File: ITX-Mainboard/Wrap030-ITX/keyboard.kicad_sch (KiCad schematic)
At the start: 4 parts, among them J13 DIN-6, U24 ATtiny2313A-PU, Y1 16M

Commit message: PCB substantial completion
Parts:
- removed J13: DIN-6, Wrap030-ITX:MiniDIN6, symbol Connector:DIN-6
- added J13: mDIN-6, Wrap030-ITX:MiniDIN6, symbol Wrap030-ITX:miniDIN-6 w/Shield
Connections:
- net GND: now also J13.0, J13.3
- net PS2-CLK: now also J13.5
- net PS2-DAT: now also J13.1
- net VCC: now also J13.4
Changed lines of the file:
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@@
     (stroke (width 0) (type default))
   )
-  (wire (pts (xy 109.22 162.56) (xy 119.38 162.56))
+  (wire (pts (xy 129.54 172.72) (xy 129.54 162.56))
     (stroke (width 0) (type default))
   )
@@
     (stroke (width 0) (type default))
   )
-  (wire (pts (xy 134.62 162.56) (xy 144.78 162.56))
+  (wire (pts (xy 137.16 149.86) (xy 147.32 149.86))
     (stroke (width 0) (type default))
   )
@@
     (effects (font (size 1.27 1.27)) (justify right bottom))
   )
-  (label "PS2-DAT" (at 109.22 162.56 0) (fields_autoplaced)
+  (label "PS2-DAT" (at 129.54 172.72 90) (fields_autoplaced)
     (effects (font (size 1.27 1.27)) (justify left bottom))
   )
@@
     (effects (font (size 1.27 1.27)) (justify left bottom))
   )
-  (label "PS2-CLK" (at 144.78 162.56 180) (fields_autoplaced)
+  (label "PS2-CLK" (at 147.32 149.86 180) (fields_autoplaced)
     (effects (font (size 1.27 1.27)) (justify right bottom))
   )
@@
     )
   )
-  (symbol (lib_id "power:VCC") (at 134.62 157.48 270) (unit 1)
-    (in_bom yes) (on_board yes) (dnp no) (fields_autoplaced)
-    (property "Reference" "#PWR03" (at 130.81 157.48 0)
-      (effects (font (size 1.27 1.27)) hide)
-    )
-    (property "Value" "VCC" (at 137.795 157.7968 90)
-      (effects (font (size 1.27 1.27)) (justify left))
-    )
-    (property "Footprint" "" (at 134.62 157.48 0)
-      (effects (font (size 1.27 1.27)) hide)
-    )
-    (property "Datasheet" "" (at 134.62 157.48 0)
+  (symbol (lib_id "power:VCC") (at 116.84 154.94 90) (unit 1)
+    (in_bom yes) (on_board yes) (dnp no) (fields_autoplaced)
+    (property "Reference" "#PWR03" (at 120.65 154.94 0)
+      (effects (font (size 1.27 1.27)) hide)
+    )
+    (property "Value" "VCC" (at 113.665 155.2568 90)
+      (effects (font (size 1.27 1.27)) (justify left))
+    )
+    (property "Footprint" "" (at 116.84 154.94 0)
+      (effects (font (size 1.27 1.27)) hide)
+    )
+    (property "Datasheet" "" (at 116.84 154.94 0)
       (effects (font (size 1.27 1.27)) hide)
     )
@@
     )
   )
-  (symbol (lib_id "power:GND") (at 127 152.4 180) (unit 1)
-    (in_bom yes) (on_board yes) (dnp no) (fields_autoplaced)
-    (property "Reference" "#PWR04" (at 127 146.05 0)
-      (effects (font (size 1.27 1.27)) hide)
-    )
-    (property "Value" "GND" (at 127 148.8981 0)
-      (effects (font (size 1.27 1.27)))
-    )
-    (property "Footprint" "" (at 127 152.4 0)
-      (effects (font (size 1.27 1.27)) hide)
-    )
-    (property "Datasheet" "" (at 127 152.4 0)
+  (symbol (lib_id "power:GND") (at 137.16 154.94 90) (unit 1)
+    (in_bom yes) (on_board yes) (dnp no) (fields_autoplaced)
+    (property "Reference" "#PWR04" (at 143.51 154.94 0)
+      (effects (font (size 1.27 1.27)) hide)
+    )
+    (property "Value" "GND" (at 140.335 155.2568 90)
+      (effects (font (size 1.27 1.27)) (justify right))
+    )
+    (property "Footprint" "" (at 137.16 154.94 0)
+      (effects (font (size 1.27 1.27)) hide)
+    )
+    (property "Datasheet" "" (at 137.16 154.94 0)
       (effects (font (size 1.27 1.27)) hide)
     )
@@
     )
   )
+  (symbol (lib_id "power:GND") (at 127 142.24 180) (unit 1)
+    (in_bom yes) (on_board yes) (dnp no) (fields_autoplaced)
+    (property "Reference" "#PWR04" (at 127 135.89 0)
+      (effects (font (size 1.27 1.27)) hide)
+    )
+    (property "Value" "GND" (at 127 138.7381 0)
+      (effects (font (size 1.27 1.27)))
+    )
+    (property "Footprint" "" (at 127 142.24 0)
+      (effects (font (size 1.27 1.27)) hide)
+    )
+    (property "Datasheet" "" (at 127 142.24 0)
+      (effects (font (size 1.27 1.27)) hide)
+    )
+    (pin "1")
+    (instances
+      (project "Wrap030-ITX"
+        (path "/911cb688-7d4c-4194-bbd3-2b645bd8d53c"
+          (reference "#PWR04") (unit 1)
+        )
+        (path "/911cb688-7d4c-4194-bbd3-2b645bd8d53c/26daa56c-062f-43fe-98ce-9d136969f1f9"
+          (reference "#PWR064") (unit 1)
+        )
+        (path "/911cb688-7d4c-4194-bbd3-2b645bd8d53c/b3cc5e75-f49f-4aac-aafa-9673c6f4863c"
+          (reference "#PWR0134") (unit 1)
+        )
+        (path "/911cb688-7d4c-4194-bbd3-2b645bd8d53c/aa0ccbb1-2ab7-4898-88a6-d9cd881bb239"
+          (reference "#PWR0174") (unit 1)
+        )
+        (path "/911cb688-7d4c-4194-bbd3-2b645bd8d53c/08245a1d-e019-4487-bc27-8c0c37f6c7e2"
+          (reference "#PWR0351") (unit 1)
+        )
+      )
+    )
+  )
   (symbol (lib_id "Device:Resonator_Small") (at 96.52 88.9 270) (unit 1)
     (in_bom yes) (on_board yes) (dnp no)
@@
     )
   )
-  (symbol (lib_id "power:VCC") (at 127 73.66 0) (unit 1)
-    (in_bom yes) (on_board yes) (dnp no) (fields_autoplaced)
-    (property "Reference" "#PWR03" (at 127 77.47 0)
-      (effects (font (size 1.27 1.27)) hide)
-    )
-    (property "Value" "VCC" (at 127 70.1581 0)
-      (effects (font (size 1.27 1.27)))
-    )
-    (property "Footprint" "" (at 127 73.66 0)
-      (effects (font (size 1.27 1.27)) hide)
-    )
-    (property "Datasheet" "" (at 127 73.66 0)
-      (effects (font (size 1.27 1.27)) hide)
-    )
-    (pin "1")
-    (instances
-      (project "Wrap030-ITX"
-        (path "/911cb688-7d4c-4194-bbd3-2b645bd8d53c"
-          (reference "#PWR03") (unit 1)
-        )
-        (path "/911cb688-7d4c-4194-bbd3-2b645bd8d53c/26daa56c-062f-43fe-98ce-9d136969f1f9"
-          (reference "#PWR063") (unit 1)
-        )
-        (path "/911cb688-7d4c-4194-bbd3-2b645bd8d53c/b3cc5e75-f49f-4aac-aafa-9673c6f4863c"
-          (reference "#PWR0133") (unit 1)
-        )
-        (path "/911cb688-7d4c-4194-bbd3-2b645bd8d53c/aa0ccbb1-2ab7-4898-88a6-d9cd881bb239"
-          (reference "#PWR0173") (unit 1)
-        )
-        (path "/911cb688-7d4c-4194-bbd3-2b645bd8d53c/08245a1d-e019-4487-bc27-8c0c37f6c7e2"
-          (reference "#PWR0333") (unit 1)
-        )
-      )
-    )
-  )
-  (symbol (lib_id "Connector:DIN-6") (at 127 160.02 0) (unit 1)
-    (in_bom yes) (on_board yes) (dnp no) (fields_autoplaced)
-    (property "Reference" "J13" (at 128.6511 151.9521 0)
-      (effects (font (size 1.27 1.27)) (justify left))
-    )
-    (property "Value" "DIN-6" (at 128.6511 153.8731 0)
-      (effects (font (size 1.27 1.27)) (justify left))
-    )
-    (property "Footprint" "Wrap030-ITX:MiniDIN6" (at 127 160.02 0)
-      (effects (font (size 1.27 1.27)) hide)
-    )
-    (property "Datasheet" "https://www.te.com/commerce/DocumentDelivery/DDEController?Action=srchrtrv&DocNm=5749266&DocType=Customer+Drawing&DocLang=English&PartCntxt=5749266-1&DocFormat=pdf" (at 127 160.02 0)
-      (effects (font (size 1.27 1.27)) hide)
-    )
-    (property "JLC-Part" "" (at 127 160.02 0)
-      (effects (font (size 1.27 1.27)) hide)
-    )
-    (property "Mouser-Part" "571-5749266-1" (at 127 160.02 0)
-      (effects (font (size 1.27 1.27)) hide)
-    )
-    (property "Notes" "" (at 127 160.02 0)
-      (effects (font (size 1.27 1.27)) hide)
-    )
+  (symbol (lib_id "Wrap030-ITX:miniDIN-6 w/Shield") (at 127 152.4 0) (unit 1)
+    (in_bom yes) (on_board yes) (dnp no) (fields_autoplaced)
+    (property "Reference" "J13" (at 128.6511 141.8971 0)
+      (effects (font (size 1.27 1.27)) (justify left))
+    )
+    (property "Value" "mDIN-6" (at 128.6511 143.8181 0)
+      (effects (font (size 1.27 1.27)) (justify left))
+    )
+    (property "Footprint" "Wrap030-ITX:MiniDIN6" (at 127 152.4 0)
+      (effects (font (size 1.27 1.27)) hide)
+    )
+    (property "Datasheet" "https://www.te.com/commerce/DocumentDelivery/DDEController?Action=srchrtrv&DocNm=5749266&DocType=Customer+Drawing&DocLang=English&PartCntxt=5749266-1&DocFormat=pdf" (at 127 152.4 0)
+      (effects (font (size 1.27 1.27)) hide)
+    )
+    (property "Mouser-Part" "571-5749266-1" (at 127 152.4 0)
+      (effects (font (size 1.27 1.27)) hide)
+    )
+    (pin "0")
     (pin "1")
     (pin "2")
@@
         )
       )
+    )
+  )
+  (symbol (lib_id "power:VCC") (at 127 73.66 0) (unit 1)
+    (in_bom yes) (on_board yes) (dnp no) (fields_autoplaced)
+    (property "Reference" "#PWR03" (at 127 77.47 0)
+      (effects (font (size 1.27 1.27)) hide)
+    )
+    (property "Value" "VCC" (at 127 70.1581 0)
+      (effects (font (size 1.27 1.27)))
+    )
+    (property "Footprint" "" (at 127 73.66 0)
+      (effects (font (size 1.27 1.27)) hide)
+    )
+    (property "Datasheet" "" (at 127 73.66 0)
+      (effects (font (size 1.27 1.27)) hide)
+    )
+    (pin "1")
+    (instances
+      (project "Wrap030-ITX"
+        (path "/911cb688-7d4c-4194-bbd3-2b645bd8d53c"
+          (reference "#PWR03") (unit 1)
+        )
+        (path "/911cb688-7d4c-4194-bbd3-2b645bd8d53c/26daa56c-062f-43fe-98ce-9d136969f1f9"
+          (reference "#PWR063") (unit 1)
+        )
+        (path "/911cb688-7d4c-4194-bbd3-2b645bd8d53c/b3cc5e75-f49f-4aac-aafa-9673c6f4863c"
+          (reference "#PWR0133") (unit 1)
+        )
+        (path "/911cb688-7d4c-4194-bbd3-2b645bd8d53c/aa0ccbb1-2ab7-4898-88a6-d9cd881bb239"
+          (reference "#PWR0173") (unit 1)
+        )
+        (path "/911cb688-7d4c-4194-bbd3-2b645bd8d53c/08245a1d-e019-4487-bc27-8c0c37f6c7e2"
+          (reference "#PWR0333") (unit 1)
+        )
+      )

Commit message: Completing PCB Routing
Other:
- title: Wrap030 ITX -> Wrap030-ATX Mainboard
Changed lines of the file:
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@@
   (paper "USLetter")
   (title_block
-    (title "Wrap030 ITX")
-    (date "2023-03-15")
-    (rev "0")
+    (title "Wrap030-ATX Mainboard")
+    (date "2023-03-26")
+    (rev "1")
     (company "techav")
   )

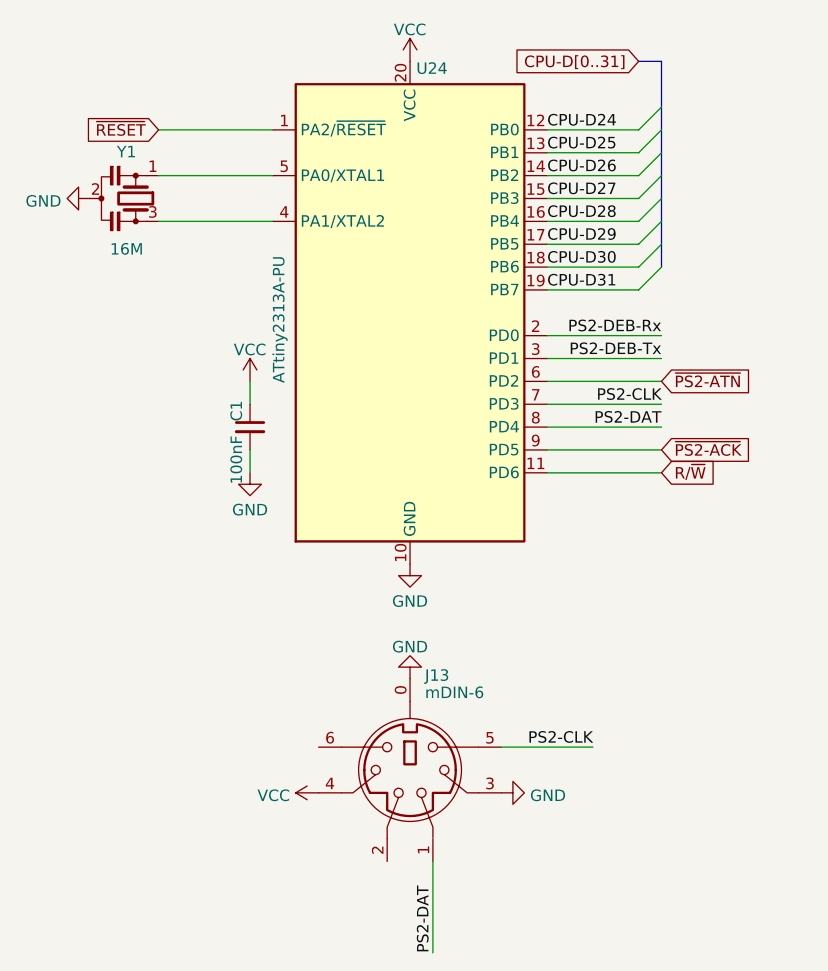
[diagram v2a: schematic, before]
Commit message: PCB Silkscreen & DRC Cleanup
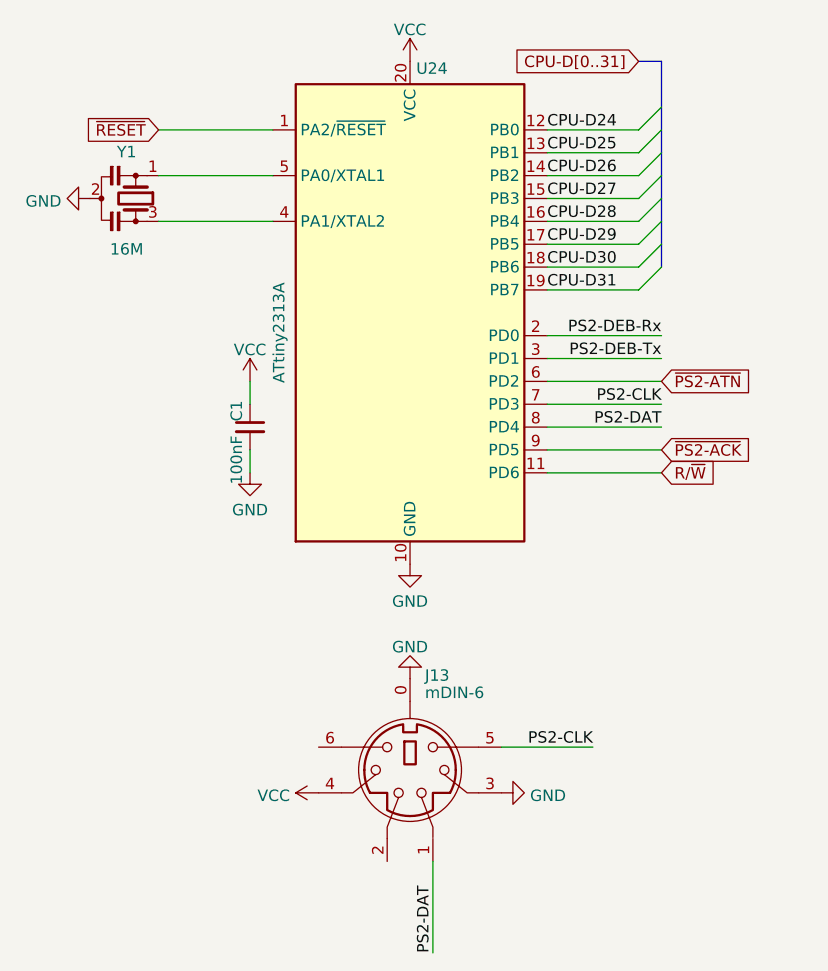
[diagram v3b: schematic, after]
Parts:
- U24: value ATtiny2313A-PU -> ATtiny2313A
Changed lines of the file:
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@@
       (effects (font (size 1.27 1.27)) (justify left))
     )
-    (property "Value" "ATtiny2313A-PU" (at 112.4459 109.4011 90)
+    (property "Value" "ATtiny2313A" (at 112.4459 109.4011 90)
       (effects (font (size 1.27 1.27)) (justify left))
     )

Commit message: Replace resistor nets with 0402 & update gerbers
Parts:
- C1: Mouser-Part (none) -> 187-CL05B104KO5NNNC; Notes (none) -> JLC
- J13: Notes (none) -> Mouser
- U24: Notes (none) -> Mouser; Socket-Mouser (none) -> 571-1-2199298-6
- Y1: Mouser-Part (none) -> 81-CSTLS16M0X55-B0; Notes (none) -> Mouser
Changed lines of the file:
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@@
       (effects (font (size 1.27 1.27)) hide)
     )
-    (property "Notes" "" (at 127 101.6 0)
+    (property "Notes" "Mouser" (at 127 101.6 0)
+      (effects (font (size 1.27 1.27)) hide)
+    )
+    (property "Socket-Mouser" "571-1-2199298-6" (at 127 101.6 0)
       (effects (font (size 1.27 1.27)) hide)
     )
@@
       (effects (font (size 1.27 1.27)) hide)
     )
-    (property "Mouser-Part" "" (at 96.52 88.9 0)
+    (property "Mouser-Part" "81-CSTLS16M0X55-B0" (at 96.52 88.9 0)
       (effects (font (size 1.27 1.27)) hide)
     )
-    (property "Notes" "" (at 96.52 88.9 0)
+    (property "Notes" "Mouser" (at 96.52 88.9 0)
+      (effects (font (size 1.27 1.27)) hide)
+    )
+    (property "Socket-Mouser" "" (at 96.52 88.9 0)
       (effects (font (size 1.27 1.27)) hide)
     )
@@
       (effects (font (size 1.27 1.27)) hide)
     )
-    (property "Mouser-Part" "" (at 109.22 114.3 0)
+    (property "Mouser-Part" "187-CL05B104KO5NNNC" (at 109.22 114.3 0)
       (effects (font (size 1.27 1.27)) hide)
     )
-    (property "Notes" "" (at 109.22 114.3 0)
+    (property "Notes" "JLC" (at 109.22 114.3 0)
+      (effects (font (size 1.27 1.27)) hide)
+    )
+    (property "Socket-Mouser" "" (at 109.22 114.3 0)
       (effects (font (size 1.27 1.27)) hide)
     )
@@
       (effects (font (size 1.27 1.27)) hide)
     )
+    (property "Notes" "Mouser" (at 127 152.4 0)
+      (effects (font (size 1.27 1.27)) hide)
+    )
+    (property "Socket-Mouser" "" (at 127 152.4 0)
+      (effects (font (size 1.27 1.27)) hide)
+    )
